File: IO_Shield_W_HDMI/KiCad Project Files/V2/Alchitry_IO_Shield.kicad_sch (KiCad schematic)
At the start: 1 part, among them U1 Alchitry_Single

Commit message: working on placement
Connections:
- net +3V3: now also U1.C_13 (3.3V), U1.C_19 (3.3V), U1.C_7 (3.3V)
- net +5V: now also U1.C_1 (Raw)
- net AN0: now also U1.B_12 (F4); no longer U1.A_43 (P9)
- net AN1: now also U1.B_11 (F3); no longer U1.A_42 (N9)
- net AN2: now also U1.B_9 (F2)
- net AN3: now also U1.B_8 (E1)
- net C0: now also U1.B_20 (B5)
- net C1: now also U1.B_21 (B6)
- net C2: now also U1.B_23 (A7); no longer U1.A_48 (T9)
- net C3: now also U1.B_24 (B7); no longer U1.A_46 (R6)
- net C4: now also U1.B_18 (A5); no longer U1.A_45 (R7)
- net C5: now also U1.B_17 (A4)
- net C6: now also U1.B_15 (B4)
- net DP: now also U1.B_14 (A3); no longer U1.A_49 (T10)
- net LED0: now also U1.C_30 (R3); no longer U1.C_27 (T4)
- net LED1: now also U1.C_34 (R1); no longer U1.C_28 (T3)
- net LED10: now also U1.C_46 (N12); no longer U1.C_42 (N13)
- net LED11: now also U1.C_2 (T13); no longer U1.C_43 (P13)
- net LED12: now also U1.C_27 (T4); no longer U1.C_45 (N11)
- net LED13: now also U1.C_31 (T2); no longer U1.C_46 (N12)
- net LED14: now also U1.C_36 (N1); no longer U1.C_48 (P10)
- net LED15: now also U1.C_40 (M1); no longer U1.C_49 (P11)
- net LED16: now also U1.C_45 (N11); no longer U1.A_24 (E6)
- net LED17: now also U1.C_49 (P11); no longer U1.A_23 (K5)
- net LED18: now also U1.A_24 (E6); no longer U1.A_21 (G2)
- net LED2: now also U1.C_39 (M2); no longer U1.C_30 (R3)
- net LED20: now also U1.A_15 (K1); no longer U1.A_18 (H2)
- net LED21: now also U1.A_11 (L2); no longer U1.A_17 (H1)
- net LED22: now also U1.A_6 (R5); no longer U1.A_15 (K1)
- net LED23: now also U1.A_2 (T8); no longer U1.A_14 (J1)
- net LED24: now also U1.A_23 (K5); no longer U1.A_12 (L3)
- net LED25: now also U1.A_18 (H2); no longer U1.A_11 (L2)
- net LED26: now also U1.A_14 (J1); no longer U1.A_9 (P8)
- net LED27: now also U1.A_9 (P8); no longer U1.A_8 (R8)
- net LED28: now also U1.A_5 (T5); no longer U1.A_6 (R5)
- net LED29: now also U1.A_48 (T9); no longer U1.A_5 (T5)
- net LED3: now also U1.C_43 (P13); no longer U1.C_31 (T2)
- net LED30: now also U1.A_21 (G2); no longer U1.A_3 (T7)
- net LED31: now also U1.A_17 (H1); no longer U1.A_2 (T8)
- net LED32: now also U1.A_12 (L3); no longer U1.A_27 (M6)
- net LED33: now also U1.A_8 (R8); no longer U1.A_28 (N6)
- net LED34: now also U1.A_3 (T7); no longer U1.A_30 (H5)
- net LED35: now also U1.A_49 (T10); no longer U1.A_31 (H4)
- net LED4: now also U1.C_48 (P10); no longer U1.C_33 (R2)
- net LED5: now also U1.C_3 (R13); no longer U1.C_34 (R1)
- net LED6: now also U1.C_28 (T3); no longer U1.C_36 (N1)
- net LED7: now also U1.C_33 (R2); no longer U1.C_37 (P1)
- net LED8: now also U1.C_37 (P1); no longer U1.C_39 (M2)
- net LED9: now also U1.C_42 (N13); no longer U1.C_40 (M1)

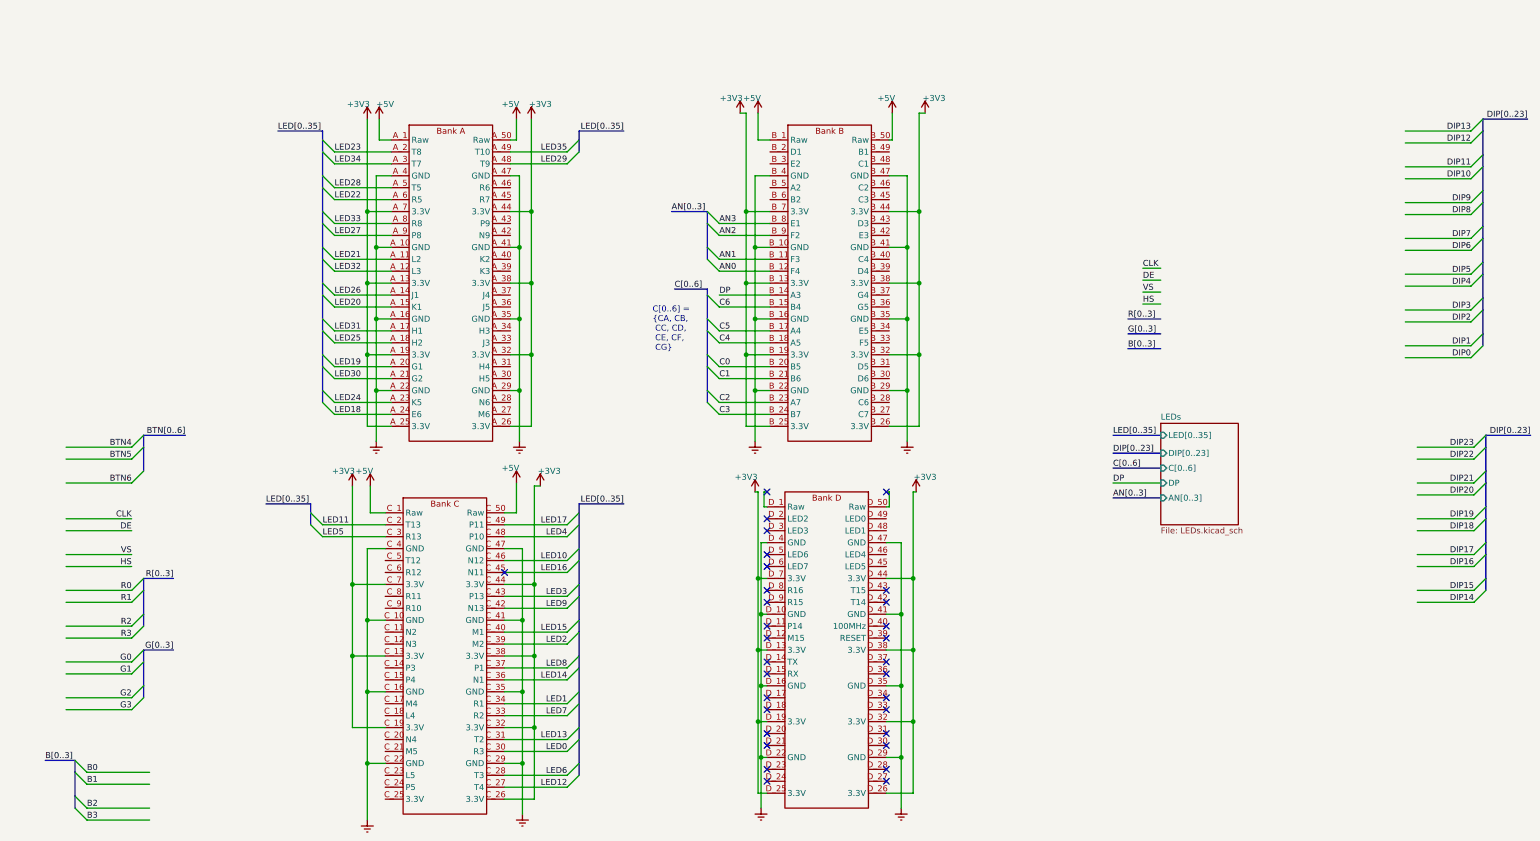
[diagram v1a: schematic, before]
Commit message: switches and 7seg routed
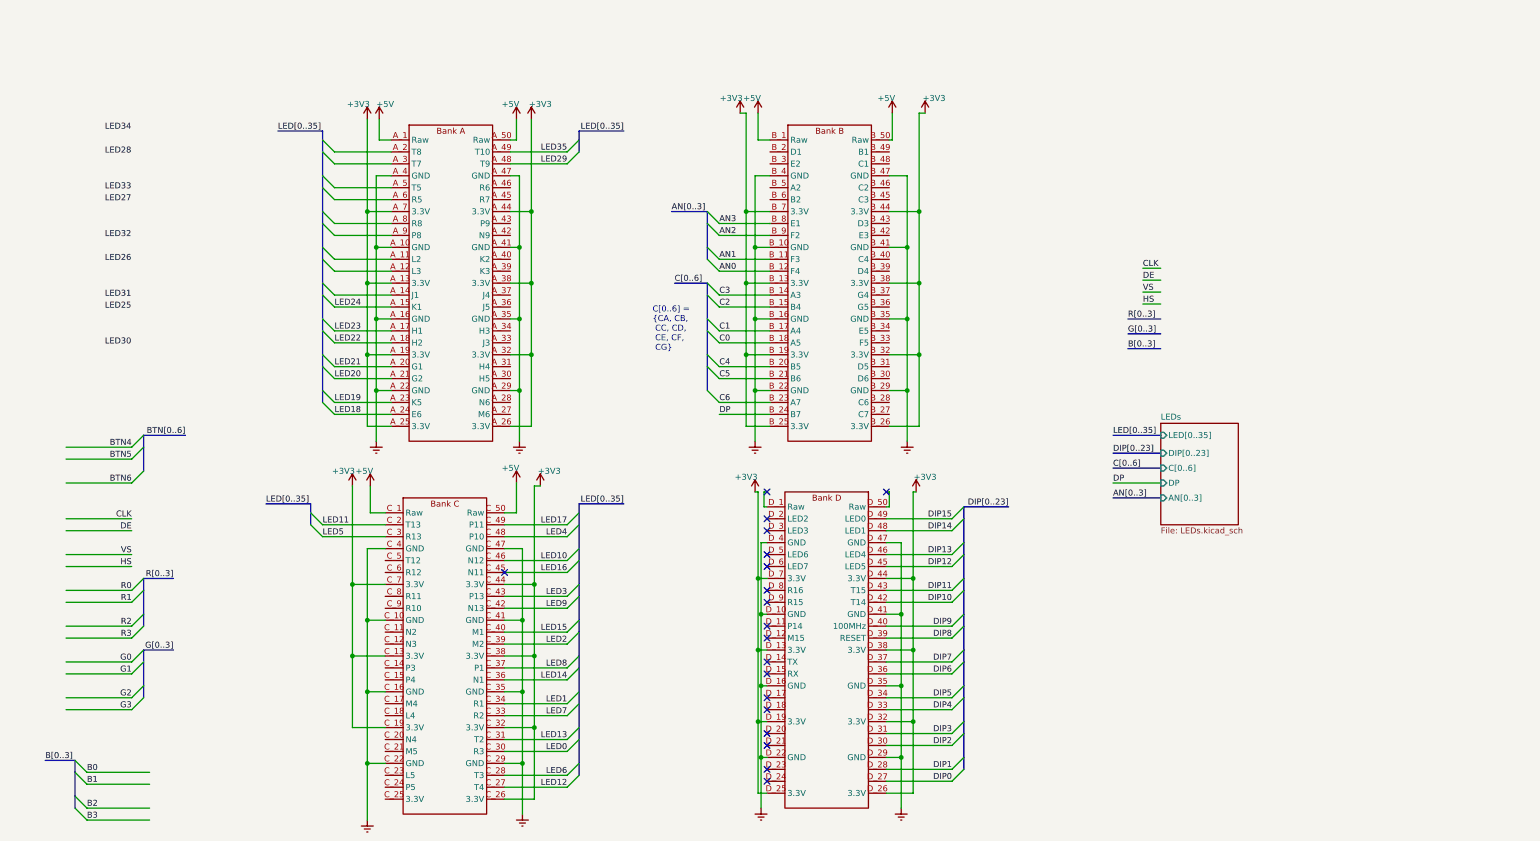
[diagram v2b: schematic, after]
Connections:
- net C0: now also U1.B_18 (A5); no longer U1.B_20 (B5)
- net C1: now also U1.B_17 (A4); no longer U1.B_21 (B6)
- net C2: now also U1.B_15 (B4); no longer U1.B_23 (A7)
- net C3: now also U1.B_14 (A3); no longer U1.B_24 (B7)
- net C4: now also U1.B_20 (B5); no longer U1.B_18 (A5)
- net C5: now also U1.B_21 (B6); no longer U1.B_17 (A4)
- net C6: now also U1.B_23 (A7); no longer U1.B_15 (B4)
- net DIP0: now also U1.D_27
- net DIP1: now also U1.D_28
- net DIP10: now also U1.D_42 (T14)
- net DIP11: now also U1.D_43 (T15)
- net DIP12: now also U1.D_45 (LED5)
- net DIP13: now also U1.D_46 (LED4)
- net DIP14: now also U1.D_48 (LED1)
- net DIP15: now also U1.D_49 (LED0)
- net DIP2: now also U1.D_30
- net DIP3: now also U1.D_31
- net DIP4: now also U1.D_33
- net DIP5: now also U1.D_34
- net DIP6: now also U1.D_36
- net DIP7: now also U1.D_37
- net DIP8: now also U1.D_39 (RESET)
- net DIP9: now also U1.D_40 (100MHz)
- net DP: now also U1.B_24 (B7); no longer U1.B_14 (A3)
- net LED19: now also U1.A_23 (K5); no longer U1.A_20 (G1)
- net LED20: now also U1.A_21 (G2); no longer U1.A_15 (K1)
- net LED21: now also U1.A_20 (G1); no longer U1.A_11 (L2)
- net LED22: now also U1.A_18 (H2); no longer U1.A_6 (R5)
- net LED23: now also U1.A_17 (H1); no longer U1.A_2 (T8)
- net LED24: now also U1.A_15 (K1); no longer U1.A_23 (K5)
- net LED25: no longer U1.A_18 (H2)
- net LED26: no longer U1.A_14 (J1)
- net LED27: no longer U1.A_9 (P8)
- net LED28: no longer U1.A_5 (T5)
- net LED30: no longer U1.A_21 (G2)
- net LED31: no longer U1.A_17 (H1)
- net LED32: no longer U1.A_12 (L3)
- net LED33: no longer U1.A_8 (R8)
- net LED34: no longer U1.A_3 (T7)
- no-connect marks 31 -> 19

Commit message: routing complete... ,maybe add button
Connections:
- net LED0: now also U1.C_42 (N13); no longer U1.C_30 (R3)
- net LED1: now also U1.C_43 (P13); no longer U1.C_34 (R1)
- net LED10: now also U1.C_39 (M2); no longer U1.C_46 (N12)
- net LED11: now also U1.C_40 (M1); no longer U1.C_2 (T13)
- net LED12: now also U1.C_2 (T13); no longer U1.C_27 (T4)
- net LED13: now also U1.C_3 (R13); no longer U1.C_31 (T2)
- net LED14: now also U1.C_27 (T4); no longer U1.C_36 (N1)
- net LED15: now also U1.C_28 (T3); no longer U1.C_40 (M1)
- net LED16: now also U1.C_30 (R3); no longer U1.C_45 (N11)
- net LED17: now also U1.C_31 (T2); no longer U1.C_49 (P11)
- net LED2: now also U1.C_45 (N11); no longer U1.C_39 (M2)
- net LED25: now also U1.A_14 (J1)
- net LED26: now also U1.A_12 (L3)
- net LED27: now also U1.A_11 (L2)
- net LED28: now also U1.A_9 (P8)
- net LED29: now also U1.A_8 (R8); no longer U1.A_48 (T9)
- net LED3: now also U1.C_46 (N12); no longer U1.C_43 (P13)
- net LED30: now also U1.A_6 (R5)
- net LED31: now also U1.A_5 (T5)
- net LED32: now also U1.A_3 (T7)
- net LED33: now also U1.A_2 (T8)
- net LED34: now also U1.A_48 (T9)
- net LED5: now also U1.C_49 (P11); no longer U1.C_3 (R13)
- net LED6: now also U1.C_33 (R2); no longer U1.C_28 (T3)
- net LED7: now also U1.C_34 (R1); no longer U1.C_33 (R2)
- net LED8: now also U1.C_36 (N1); no longer U1.C_37 (P1)
- net LED9: now also U1.C_37 (P1); no longer U1.C_42 (N13)
- removed net +5V: U1.A_1 (Raw), U1.A_50 (Raw), U1.B_1 (Raw), U1.B_50 (Raw), U1.C_1 (Raw), U1.C_50 (Raw)
- no-connect marks 19 -> 25

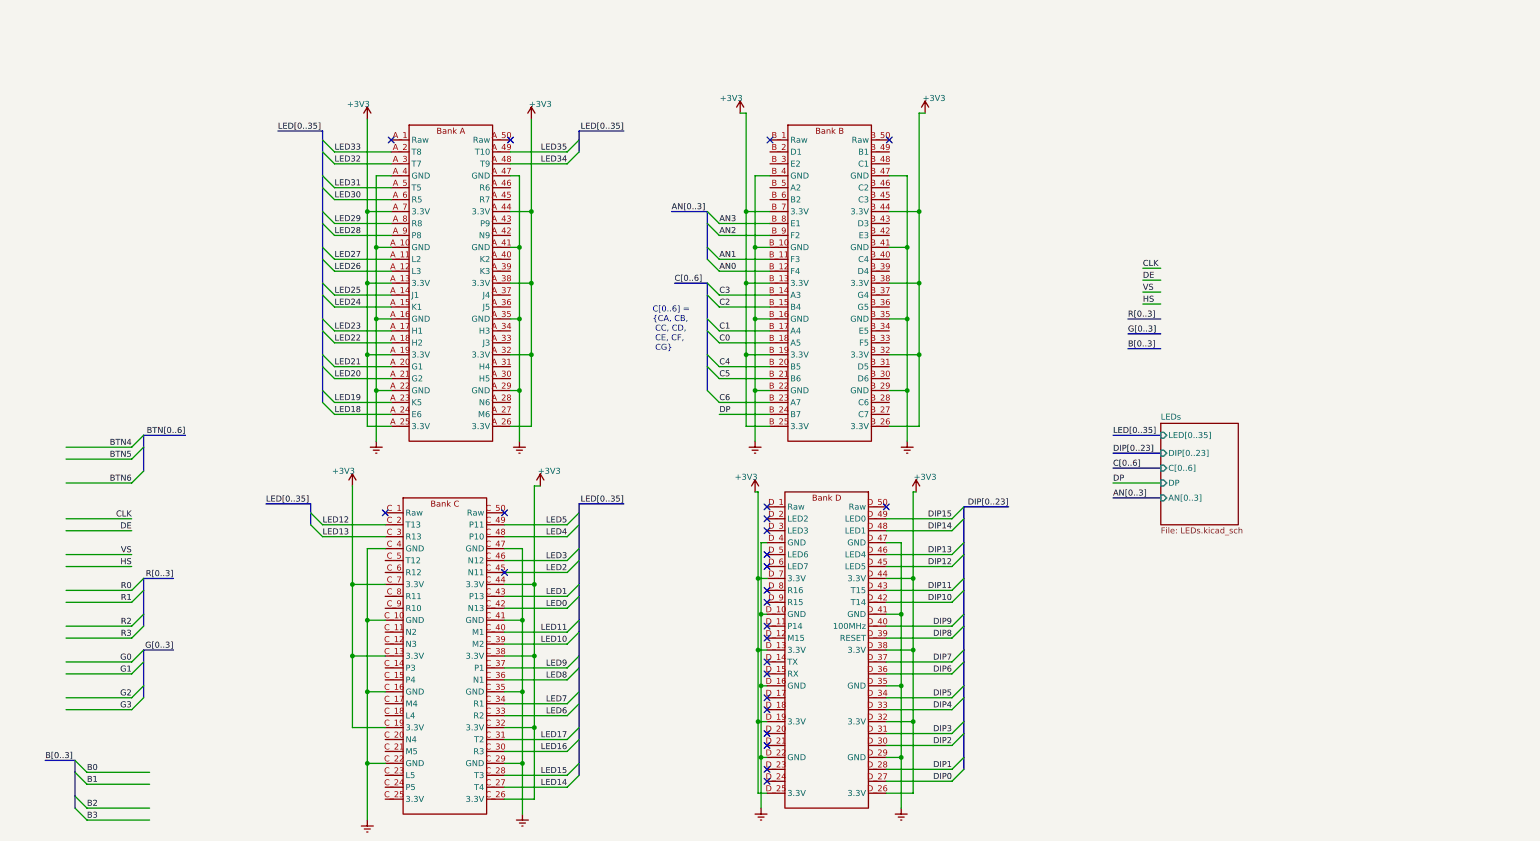
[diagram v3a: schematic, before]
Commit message: added push butttons
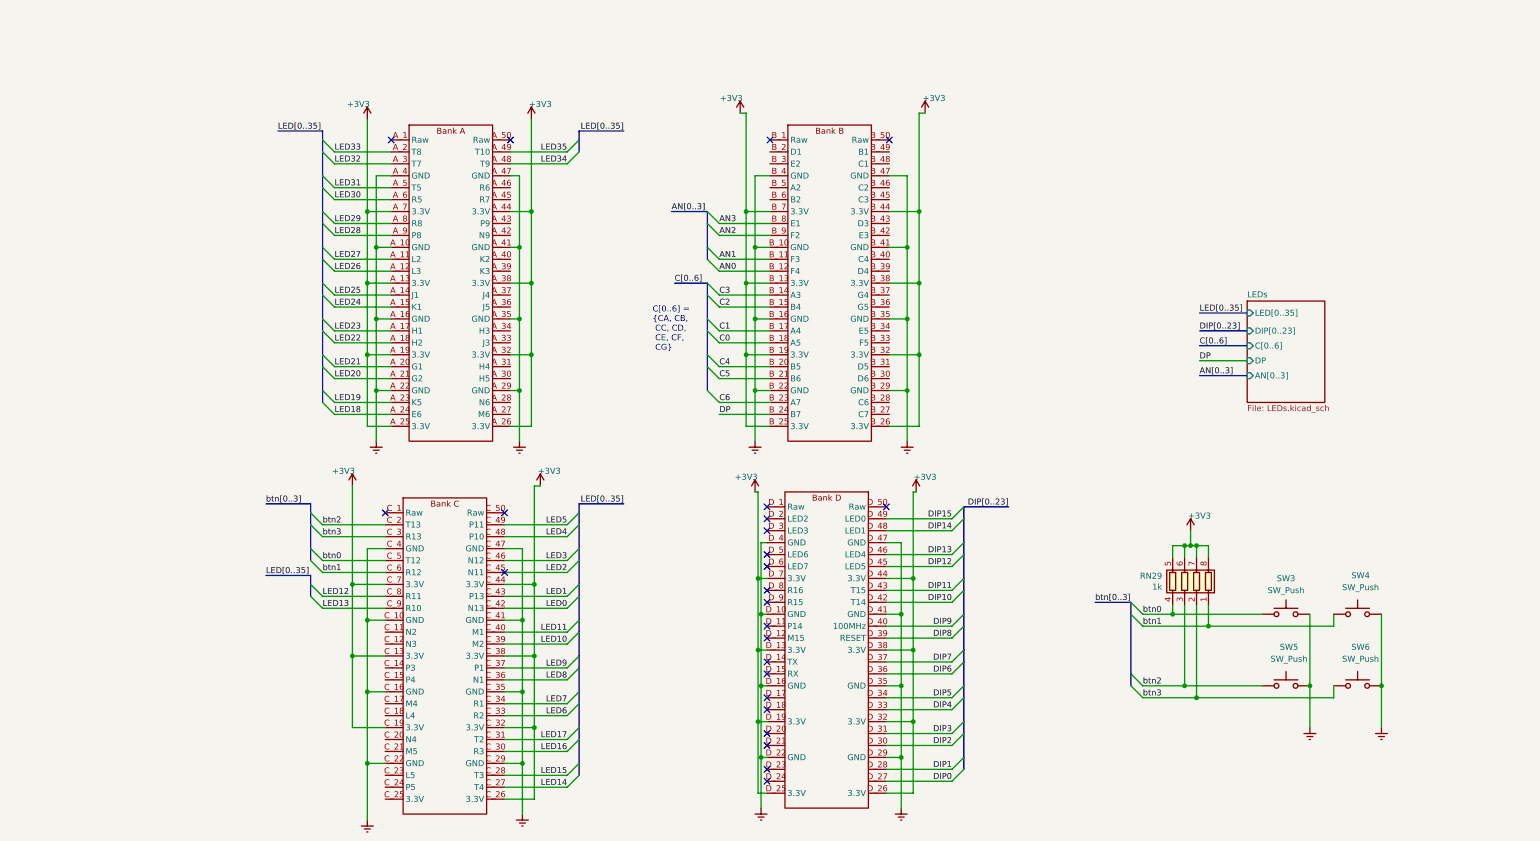
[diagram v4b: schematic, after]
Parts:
- added RN29: 1k, Resistor_SMD:R_Array_Convex_4x0603, symbol Device:R_Pack04
- added SW3, SW4, SW5, SW6: SW_Push, Button_Switch_SMD:SW_SPST_TL3342, symbol Switch:SW_Push
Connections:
- net +3V3: now also RN29.5 (R4.2), RN29.6 (R3.2), RN29.7 (R2.2), RN29.8 (R1.2)
- net GNDREF: now also SW3.2, SW4.2, SW5.2, SW6.2
- net LED12: now also U1.C_8 (R11); no longer U1.C_2 (T13)
- net LED13: now also U1.C_9 (R10); no longer U1.C_3 (R13)
- net btn0: now reaches U1.C_5 (T12)
- net btn0: now also RN29.4 (R4.1), SW3.1
- net btn1: now reaches U1.C_6 (R12)
- net btn1: now also RN29.1 (R1.1), SW4.1
- new net btn2: RN29.3 (R3.1), SW5.1, U1.C_2 (T13)
- new net btn3: RN29.2 (R2.1), SW6.1, U1.C_3 (R13)
